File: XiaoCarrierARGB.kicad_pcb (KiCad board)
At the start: 4 copper layers, 63.5 x 38.1 mm, 44 parts, among them J1 V_{IN}^{10-24V}, J2 Conn_01x08, J3 Conn_01x01, J4 Conn_01x08, J5 Conn_01x01, J6 Conn_01x06, U1 TLV75733PDBV, U2 TPP362083-T6TR, U3 XIAO-ESP32-C6-DIP, U4 74LVC1T45W6-7, U5 74LVC1T45W6-7, U6 74LVC1T45W6-7

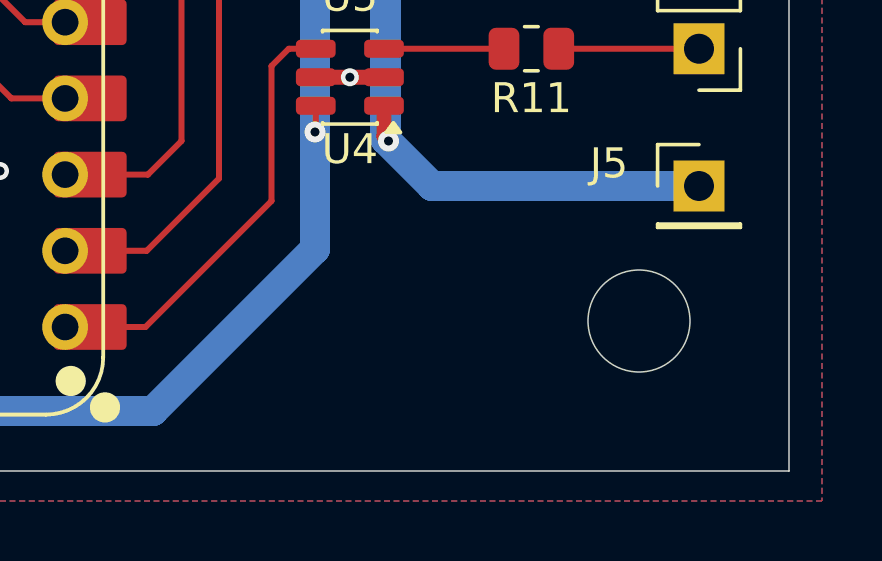
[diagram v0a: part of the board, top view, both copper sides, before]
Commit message: changed net colors
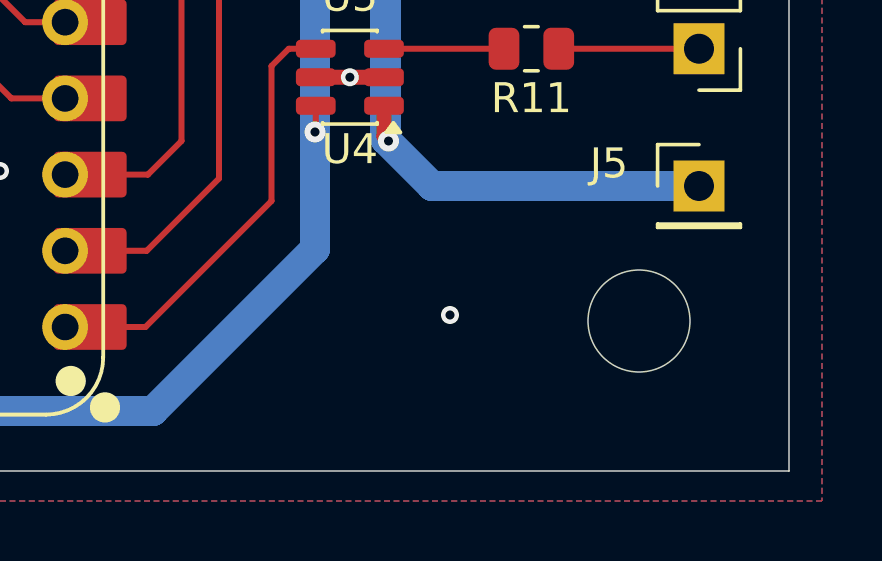
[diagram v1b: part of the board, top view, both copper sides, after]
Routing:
- net GND: vias 45 -> 46
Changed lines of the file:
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@@
+	)
+	(via
+		(at 140.45 113.85)
+		(size 0.6)
+		(drill 0.3)
+		(layers "F.Cu" "B.Cu")
+		(free yes)
+		(net "GND")
 	)
 	(via

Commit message: started GPIO silk marking table
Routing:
- net GND: vias 46 -> 55

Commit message: Did GPIO numbering Table on Fsilk
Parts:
- moved R11 1.71 mm to (141.4, 105.0)
- moved R12 1.71 mm to (141.4, 99.9)
- moved R13 1.71 mm to (141.4, 94.8)
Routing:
- net /LED_DATA^{3}: track 4.00 -> 2.29 mm
- net /LED_DATA^{2}: track 4.00 -> 2.29 mm
- net /LED_DATA^{1}: track 4.00 -> 2.29 mm
- net Net-(J6-Pin_5): track 4.68 -> 6.39 mm
- net Net-(J6-Pin_3): track 4.68 -> 6.39 mm
- net Net-(J6-Pin_1): track 4.68 -> 6.39 mm
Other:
- board text added: "C^{6} S^{3}"
- board text added: "S^{3} C^{6}"

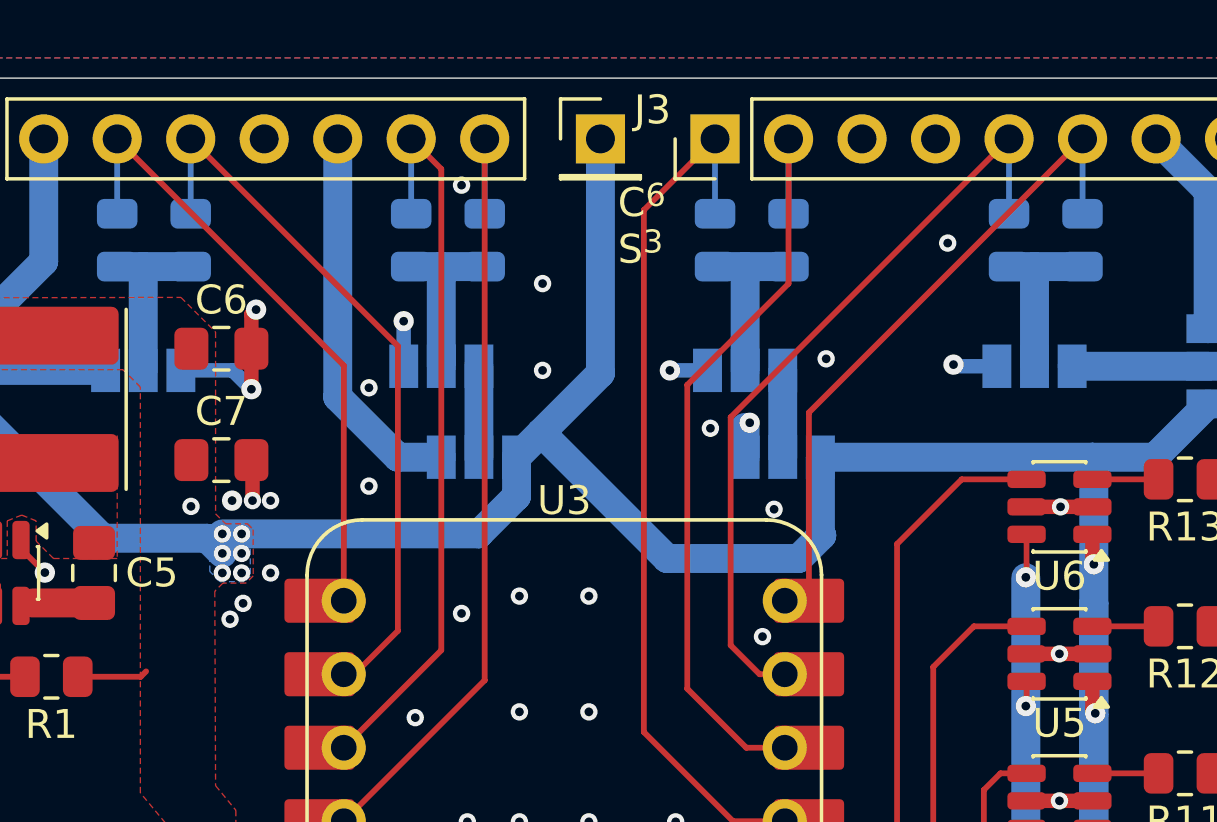
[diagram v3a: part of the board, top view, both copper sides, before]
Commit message: Rework on 3v3 gpio breakout traces maybe switch thick trace to pour on inner layer
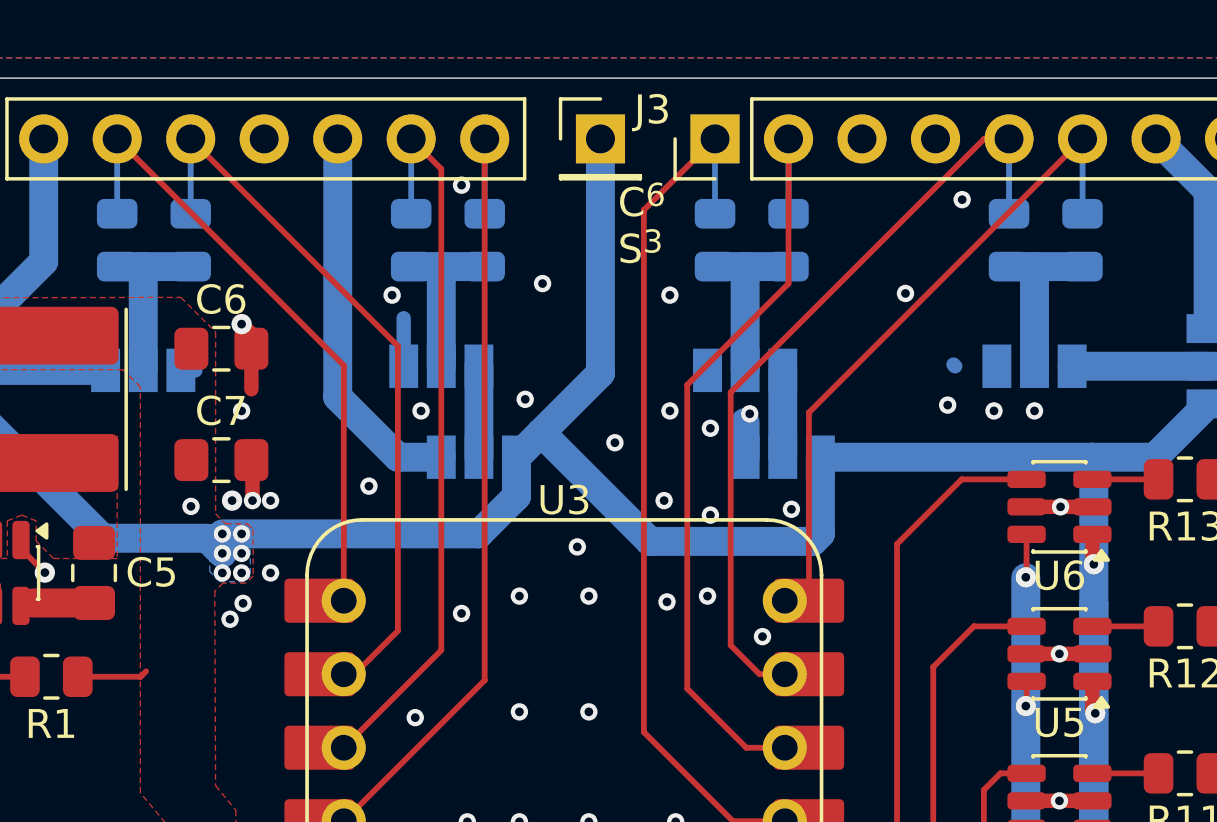
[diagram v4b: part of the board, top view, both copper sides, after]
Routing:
- net +3V3: track 153.7 -> 127.3 mm
- net GND: track 36.8 -> 31.6 mm, vias 55 -> 64
- net +5V: track 103.4 -> 102.8 mm
- net /GPIO23: track 25.9 -> 26.4 mm
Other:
- board text added: "3V3"
- board text added: "5V"
- board text added: "GND"
- board text added: "V^{+}"

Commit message: finalized design
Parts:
- added ?: Sneeble, Custom_Library:Sneeble, B.Cu at (120.8, 107.9)
- added G***: LOGO, Custom_Library:Seele_silkscreen, F.Cu at (120.0, 106.6)
- added REF**: SerbTek mark, Custom_Library:SerbTek mark, F.Cu at (100.5, 117.8)
- added REF**: SerbTek mark, Custom_Library:SerbTek mark, B.Cu at (99.7, 117.9)
- added RT**: RT-NY, RT-NY:RT-NY-Patch, F.Cu at (139.8, 113.0)
- moved JP10 7.80 mm to (106.8, 94.0), turned to 0 degrees
- moved JP14 5.65 mm to (137.6, 94.0), turned to 180 degrees
- turned JP11 to 180 degrees
- turned JP12 to 0 degrees
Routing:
- net GND: track 31.6 -> 13.3 mm, vias 64 -> 87
- net +5V: track 102.8 -> 97.5 mm
- net /Xiao3v3: track 47.9 -> 49.9 mm
- net Net-(JP10-C): track 4.60 -> 3.00 mm
- net Net-(JP14-C): track 4.70 -> 3.14 mm
- net +3V3: track 127.3 -> 128.7 mm, vias 7 -> 6
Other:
- outline, holes or cut-outs redrawn
